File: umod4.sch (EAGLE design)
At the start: 73 parts, among them IC3 27C256-FEED-THRU, J1 DMSAT-SF-PEJ, J2 10118194-0001LF, J4 CORTEX_DEBUG-PTH, J5 C160394/JST BM08B-SRSS, J6 CORTEX_DEBUG-PTH, M1 RPi Pico W, M2 Generic single-sided NEO-8, Q1 C10487/SI2301CDS, Q2 C2150/SS8050, U1 C113281/74LVC541, U2 C6091/74LVC4245, U3 C113281/74LVC541, U4 C2040/RP2040, U5 C97521/W25Q128JVSIQ, U6 C10428/74LVC2G04, U7 C10428/74LVC2G04, Y1 C9002/12MHz

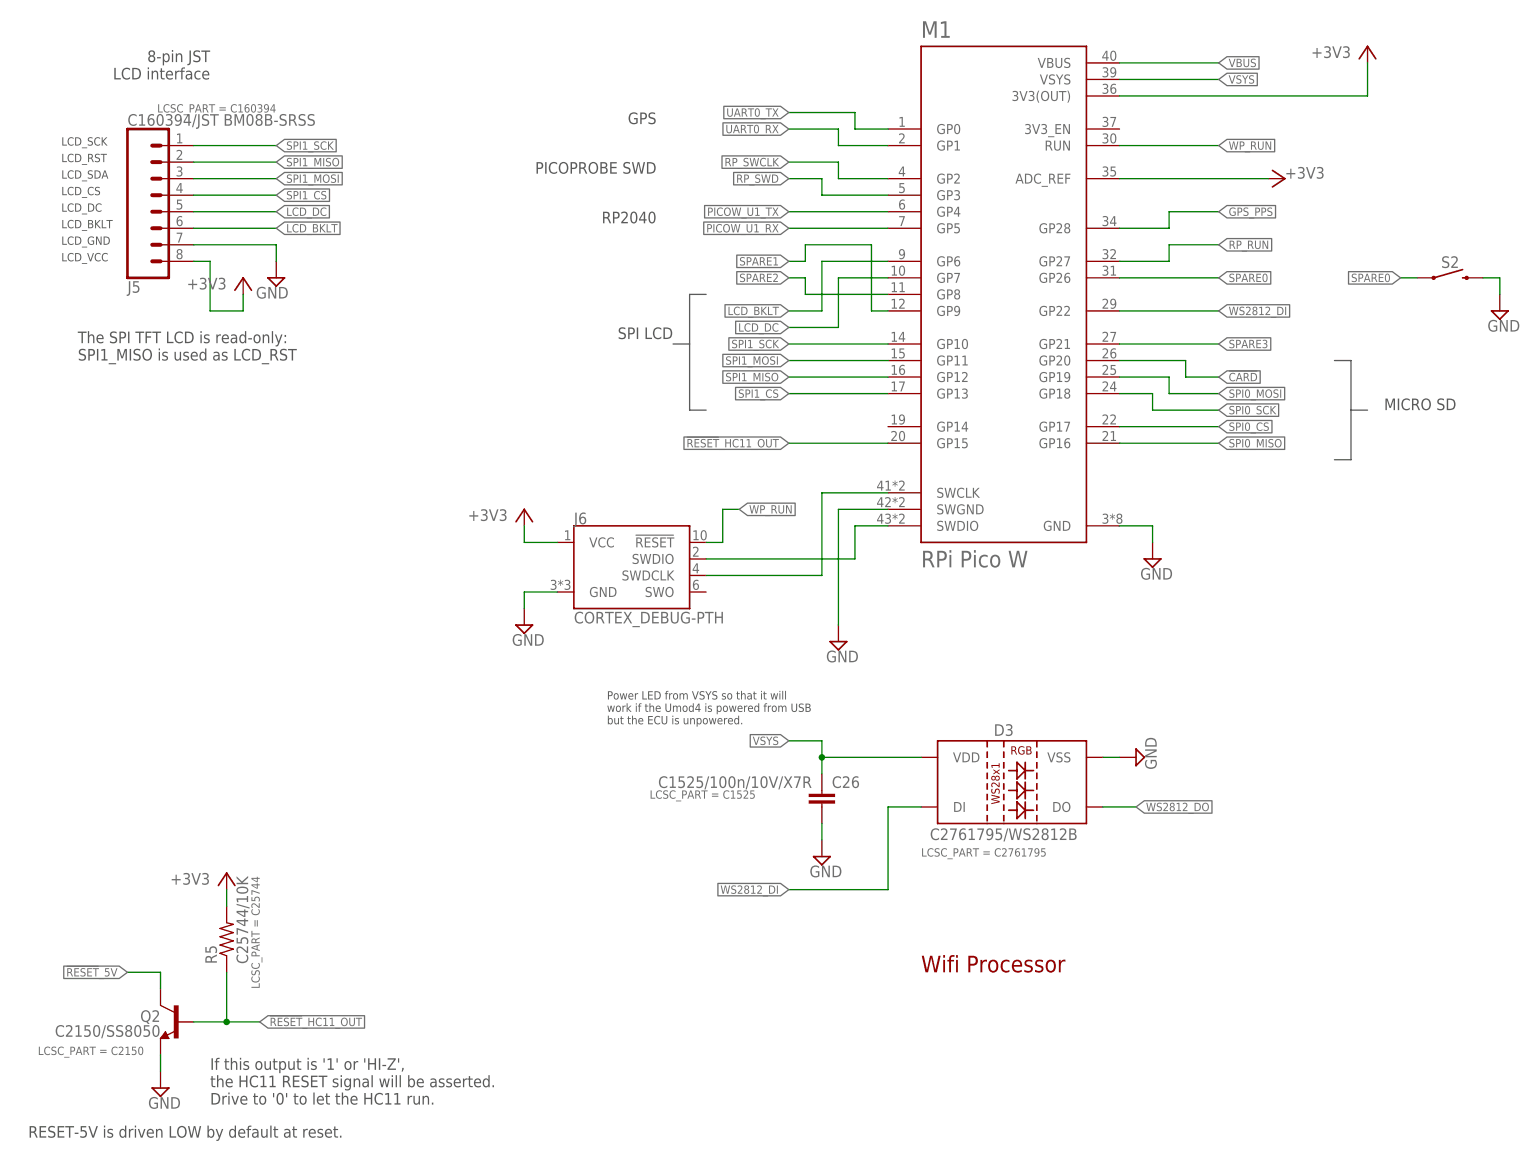
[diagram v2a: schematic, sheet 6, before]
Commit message: Added WP squid pins
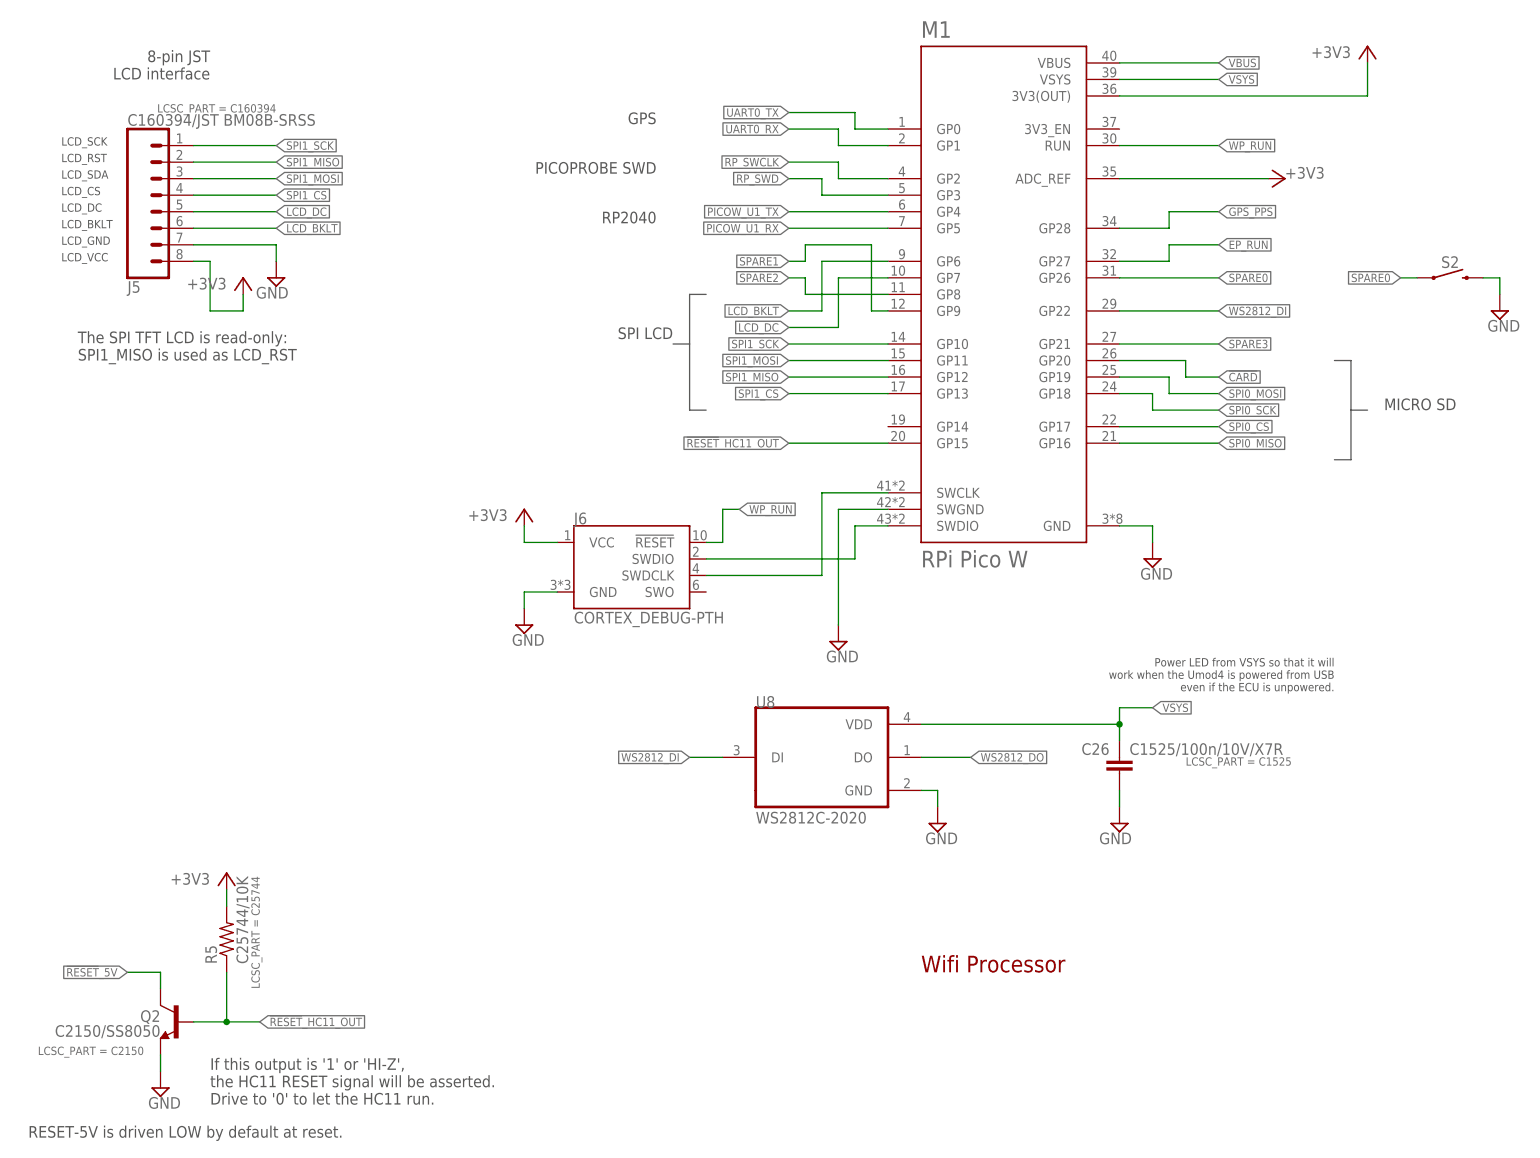
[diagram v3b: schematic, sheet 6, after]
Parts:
- removed D3: C2761795/WS2812B, SparkFun-LED:WS2812B
- added U8: WS2812C-2020, robins-v7:WS2812-2020
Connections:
- net RP_RUN renamed EP_RUN
- net GND: now also U8.GND; no longer D3.VSS
- net VSYS: now also U8.VDD; no longer D3.VDD
- net WS2812_DI: now also U8.DI; no longer D3.DI
- net WS2812_DO: now also U8.DO; no longer D3.DO
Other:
- note added: "Power LED from VSYS so that it will work when the Umod4 is powered from USB even if the ECU is unpowered."
- note removed: "Power LED from VSYS so that it will work if the Umod4 is powered from USB but the ECU is unpowered."
- moved on the sheet: C26
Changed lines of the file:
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@@
 <part name="SUPPLY21" library="supply2" deviceset="GND" device=""/>
 <part name="+3V19" library="supply1" deviceset="+3V3" device=""/>
-<part name="V13" library="supply2" deviceset="GND" device=""/>
-<part name="D3" library="SparkFun-LED" deviceset="WS2812B" device="" value="C2761795/WS2812B">
-<attribute name="LCSC_PART" value="C2761795"/>
-</part>
 <part name="C26" library="SparkFun-03-01-2010" deviceset="CAP" device="0402-CAP" value="C1525/100n/10V/X7R">
 <attribute name="LCSC_PART" value="C1525"/>
@@
 <part name="V30" library="supply2" deviceset="GND" device=""/>
 <part name="+3V24" library="supply1" deviceset="+3V3" device=""/>
+<part name="U8" library="robins-v7" deviceset="WS2812" device="-2020" value="WS2812C-2020"/>
+<part name="V41" library="supply2" deviceset="GND" device=""/>
 </parts>
 <sheets>
@@
 </segment>
 </net>
-<net name="RP_RUN" class="0">
+<net name="EP_RUN" class="0">
 <segment>
 <wire x1="119.38" y1="73.66" x2="104.14" y2="73.66" width="0.1524" layer="91"/>
@@
 the HC11 RESET signal will be asserted.
 Drive to '0' to let the HC11 run.</text>
-<text x="101.6" y="66.04" size="1.27" layer="97">Power LED from VSYS so that it will
-work if the Umod4 is powered from USB
-but the ECU is unpowered.</text>
+<text x="213.36" y="71.12" size="1.27" layer="97" rot="MR0">Power LED from VSYS so that it will
+work when the Umod4 is powered from USB
+even if the ECU is unpowered.</text>
 <text x="20.32" y="121.92" size="1.778" layer="97">The SPI TFT LCD is read-only:
 SPI1_MISO is used as LCD_RST</text>
@@
 <attribute name="VALUE" x="43.18" y="134.62" size="1.778" layer="96" rot="R180"/>
 </instance>
-<instance part="V13" gate="GND" x="182.88" y="60.96" rot="R90"/>
-<instance part="D3" gate="G$1" x="165.1" y="55.88">
-<attribute name="LCSC_PART" x="149.86" y="45.72" size="1.27" layer="96" display="both"/>
-</instance>
-<instance part="C26" gate="G$1" x="134.62" y="53.34" smashed="yes">
-<attribute name="NAME" x="136.144" y="56.261" size="1.778" layer="95"/>
-<attribute name="VALUE" x="133.096" y="58.039" size="1.778" layer="96" rot="R180"/>
-<attribute name="LCSC_PART" x="124.46" y="55.88" size="1.27" layer="96" rot="R180" display="both"/>
-</instance>
-<instance part="V34" gate="GND" x="134.62" y="45.72"/>
+<instance part="C26" gate="G$1" x="180.34" y="58.42" smashed="yes" rot="MR0">
+<attribute name="NAME" x="178.816" y="61.341" size="1.778" layer="95" rot="MR0"/>
+<attribute name="VALUE" x="181.864" y="63.119" size="1.778" layer="96" rot="MR180"/>
+<attribute name="LCSC_PART" x="190.5" y="60.96" size="1.27" layer="96" rot="MR180" display="both"/>
+</instance>
+<instance part="V34" gate="GND" x="180.34" y="50.8" rot="MR0"/>
 <instance part="Q2" gate="G$1" x="35.56" y="20.32" rot="MR0">
 <attribute name="LCSC_PART" x="30.48" y="15.24" size="1.27" layer="96" rot="MR0" display="both"/>
@@
 <attribute name="VALUE" x="205.74" y="149.86" size="1.778" layer="96"/>
 </instance>
+<instance part="U8" gate="G$1" x="134.62" y="60.96"/>
+<instance part="V41" gate="GND" x="152.4" y="50.8"/>
 </instances>
 <busses>
@@
 </segment>
 <segment>
-<wire x1="177.8" y1="60.96" x2="180.34" y2="60.96" width="0.1524" layer="91"/>
-<pinref part="V13" gate="GND" pin="GND"/>
-<pinref part="D3" gate="G$1" pin="VSS"/>
-</segment>
-<segment>
 <pinref part="C26" gate="G$1" pin="2"/>
-<wire x1="134.62" y1="50.8" x2="134.62" y2="48.26" width="0.1524" layer="91"/>
+<wire x1="180.34" y1="55.88" x2="180.34" y2="53.34" width="0.1524" layer="91"/>
 <pinref part="V34" gate="GND" pin="GND"/>
 </segment>
@@
 <wire x1="88.9" y1="86.36" x2="88.9" y2="83.82" width="0.1524" layer="91"/>
 <pinref part="V30" gate="GND" pin="GND"/>
+</segment>
+<segment>
+<pinref part="U8" gate="G$1" pin="GND"/>
+<wire x1="149.86" y1="55.88" x2="152.4" y2="55.88" width="0.1524" layer="91"/>
+<wire x1="152.4" y1="55.88" x2="152.4" y2="53.34" width="0.1524" layer="91"/>
+<pinref part="V41" gate="GND" pin="GND"/>
 </segment>
 </net>
@@
 </segment>
 </net>
-<net name="RP_RUN" class="0">
+<net name="EP_RUN" class="0">
 <segment>
 <label x="195.58" y="139.7" size="1.27" layer="95" xref="yes"/>
@@
 <segment>
 <pinref part="C26" gate="G$1" pin="1"/>
-<wire x1="134.62" y1="58.42" x2="134.62" y2="60.96" width="0.1524" layer="91"/>
-<pinref part="D3" gate="G$1" pin="VDD"/>
-<wire x1="134.62" y1="60.96" x2="149.86" y2="60.96" width="0.1524" layer="91"/>
-<wire x1="134.62" y1="60.96" x2="134.62" y2="63.5" width="0.1524" layer="91"/>
-<junction x="134.62" y="60.96"/>
-<wire x1="134.62" y1="63.5" x2="129.54" y2="63.5" width="0.1524" layer="91"/>
-<label x="129.54" y="63.5" size="1.27" layer="95" rot="R180" xref="yes"/>
+<wire x1="180.34" y1="63.5" x2="180.34" y2="66.04" width="0.1524" layer="91"/>
+<wire x1="180.34" y1="66.04" x2="180.34" y2="68.58" width="0.1524" layer="91"/>
+<junction x="180.34" y="66.04"/>
+<wire x1="180.34" y1="68.58" x2="185.42" y2="68.58" width="0.1524" layer="91"/>
+<label x="185.42" y="68.58" size="1.27" layer="95" rot="MR180" xref="yes"/>
+<pinref part="U8" gate="G$1" pin="VDD"/>
+<wire x1="180.34" y1="66.04" x2="149.86" y2="66.04" width="0.1524" layer="91"/>
 </segment>
 </net>
@@
 <net name="WS2812_DI" class="0">
 <segment>
-<wire x1="149.86" y1="53.34" x2="144.78" y2="53.34" width="0.1524" layer="91"/>
-<wire x1="144.78" y1="53.34" x2="144.78" y2="40.64" width="0.1524" layer="91"/>
-<wire x1="144.78" y1="40.64" x2="129.54" y2="40.64" width="0.1524" layer="91"/>
-<label x="129.54" y="40.64" size="1.27" layer="95" rot="R180" xref="yes"/>
-<pinref part="D3" gate="G$1" pin="DI"/>
+<wire x1="119.38" y1="60.96" x2="114.3" y2="60.96" width="0.1524" layer="91"/>
+<label x="114.3" y="60.96" size="1.27" layer="95" rot="R180" xref="yes"/>
+<pinref part="U8" gate="G$1" pin="DI"/>
 </segment>
 <segment>
@@
 <net name="WS2812_DO" class="0">
 <segment>
-<pinref part="D3" gate="G$1" pin="DO"/>
-<wire x1="177.8" y1="53.34" x2="182.88" y2="53.34" width="0.1524" layer="91"/>
-<label x="182.88" y="53.34" size="1.27" layer="95" xref="yes"/>
-</segment>
-</net>
+<label x="157.48" y="60.96" size="1.27" layer="95" xref="yes"/>
+<pinref part="U8" gate="G$1" pin="DO"/>
+<wire x1="149.86" y1="60.96" x2="157.48" y2="60.96" width="0.1524" layer="91"/>
+</segment>
+</net>

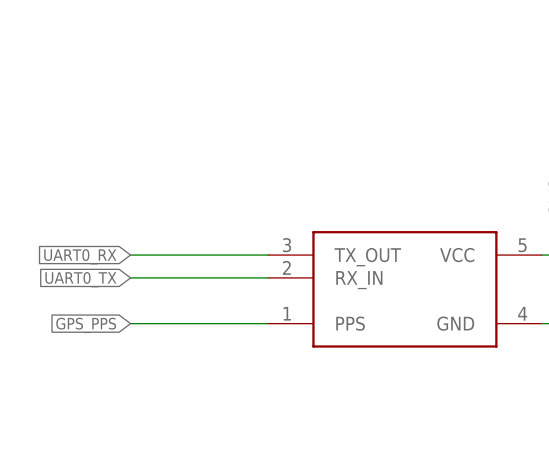
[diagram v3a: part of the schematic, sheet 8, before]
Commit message: Pullup Stops GPS From Disabling Its UART
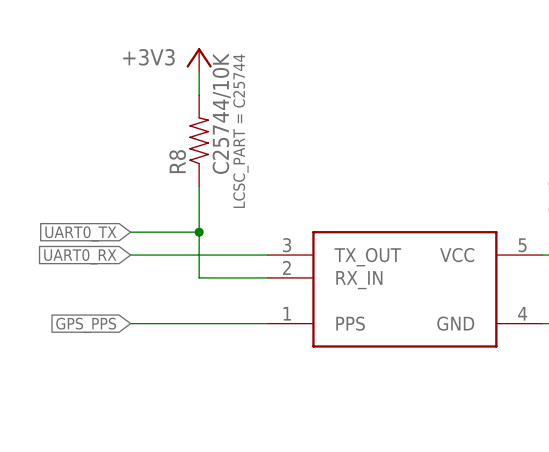
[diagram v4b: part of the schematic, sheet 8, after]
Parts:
- added R8: C25744/10K, SparkFun-03-01-2010:RESISTOR0402-RES
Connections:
- net +3V3: now also R8.2
- net UART0_TX: now also R8.1
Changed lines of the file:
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@@
 <setting verticaltext="up"/>
 </settings>
-<grid distance="0.1" unitdist="inch" unit="inch" style="lines" multiple="1" display="no" altdistance="0.01" altunitdist="inch" altunit="inch"/>
+<grid distance="0.1" unitdist="inch" unit="inch" style="lines" multiple="1" display="yes" altdistance="0.01" altunitdist="inch" altunit="inch"/>
 <layers>
 <layer number="1" name="Top" color="4" fill="1" visible="no" active="no"/>
@@
 <part name="U8" library="robins-v7" deviceset="WS2812" device="-2020" value="WS2812C-2020"/>
 <part name="V41" library="supply2" deviceset="GND" device=""/>
+<part name="+3V20" library="supply1" deviceset="+3V3" device=""/>
+<part name="R8" library="SparkFun-03-01-2010" deviceset="RESISTOR" device="0402-RES" value="C25744/10K">
+<attribute name="LCSC_PART" value="C25744"/>
+</part>
 </parts>
 <sheets>
@@
 <text x="17.78" y="139.7" size="1.27" layer="97">LCD_GND</text>
 <text x="17.78" y="137.16" size="1.27" layer="97">LCD_VCC</text>
+<wire x1="139.7" y1="157.48" x2="140.97" y2="158.75" width="0.1524" layer="97"/>
+<wire x1="139.7" y1="157.48" x2="140.97" y2="156.21" width="0.1524" layer="97"/>
+<wire x1="139.7" y1="156.21" x2="140.97" y2="154.94" width="0.1524" layer="97"/>
+<wire x1="140.97" y1="154.94" x2="139.7" y2="153.67" width="0.1524" layer="97"/>
 </plain>
 <instances>
@@
 <segment>
 <label x="129.54" y="160.02" size="1.27" layer="95" rot="R180" xref="yes"/>
-<wire x1="139.7" y1="160.02" x2="129.54" y2="160.02" width="0.1524" layer="91"/>
-<wire x1="139.7" y1="160.02" x2="139.7" y2="157.48" width="0.1524" layer="91"/>
+<wire x1="137.16" y1="160.02" x2="129.54" y2="160.02" width="0.1524" layer="91"/>
+<wire x1="137.16" y1="160.02" x2="137.16" y2="157.48" width="0.1524" layer="91"/>
 <pinref part="M1" gate="G$1" pin="GP0"/>
-<wire x1="139.7" y1="157.48" x2="144.78" y2="157.48" width="0.1524" layer="91"/>
+<wire x1="137.16" y1="157.48" x2="144.78" y2="157.48" width="0.1524" layer="91"/>
 </segment>
 </net>
@@
 <segment>
 <label x="129.54" y="157.48" size="1.27" layer="95" rot="R180" xref="yes"/>
-<wire x1="137.16" y1="157.48" x2="129.54" y2="157.48" width="0.1524" layer="91"/>
-<wire x1="137.16" y1="157.48" x2="137.16" y2="154.94" width="0.1524" layer="91"/>
+<wire x1="134.62" y1="157.48" x2="129.54" y2="157.48" width="0.1524" layer="91"/>
+<wire x1="134.62" y1="157.48" x2="134.62" y2="154.94" width="0.1524" layer="91"/>
 <pinref part="M1" gate="G$1" pin="GP1"/>
-<wire x1="137.16" y1="154.94" x2="144.78" y2="154.94" width="0.1524" layer="91"/>
+<wire x1="134.62" y1="154.94" x2="144.78" y2="154.94" width="0.1524" layer="91"/>
 </segment>
 </net>
@@
 <instance part="V33" gate="GND" x="137.16" y="101.6"/>
 <instance part="+3V18" gate="G$1" x="137.16" y="121.92"/>
+<instance part="+3V20" gate="G$1" x="93.98" y="137.16" smashed="yes">
+<attribute name="VALUE" x="91.44" y="137.16" size="1.778" layer="96" rot="R180"/>
+</instance>
+<instance part="R8" gate="G$1" x="93.98" y="127" rot="R90">
+<attribute name="LCSC_PART" x="99.06" y="119.38" size="1.27" layer="96" rot="R90" display="both"/>
+</instance>
 </instances>
 <busses>
@@
 <wire x1="137.16" y1="114.3" x2="132.08" y2="114.3" width="0.1524" layer="91"/>
 </segment>
+<segment>
+<wire x1="93.98" y1="132.08" x2="93.98" y2="134.62" width="0.1524" layer="91"/>
+<pinref part="+3V20" gate="G$1" pin="+3V3"/>
+<pinref part="R8" gate="G$1" pin="2"/>
+</segment>
 </net>
 <net name="GND" class="0">
@@
 <segment>
 <pinref part="M2" gate="G$1" pin="RX_IN"/>
-<wire x1="101.6" y1="111.76" x2="86.36" y2="111.76" width="0.1524" layer="91"/>
-<label x="86.36" y="111.76" size="1.27" layer="95" rot="R180" xref="yes"/>
+<wire x1="101.6" y1="111.76" x2="93.98" y2="111.76" width="0.1524" layer="91"/>
+<wire x1="93.98" y1="111.76" x2="93.98" y2="116.84" width="0.1524" layer="91"/>
+<wire x1="93.98" y1="116.84" x2="86.36" y2="116.84" width="0.1524" layer="91"/>
+<label x="86.36" y="116.84" size="1.27" layer="95" rot="R180" xref="yes"/>
+<pinref part="R8" gate="G$1" pin="1"/>
+<wire x1="93.98" y1="116.84" x2="93.98" y2="121.92" width="0.1524" layer="91"/>
+<junction x="93.98" y="116.84"/>
 </segment>
 </net>

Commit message: Latest updates. See ChangeList.md.
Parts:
- added C13: 4.7uF/25V, robins-v7:CAP-0603
- added C28, C29: 0.1uF/25V, robins-v7:CAP-0603
- added C30, C31: 10uF/10V, robins-v7:CAP-0805
- added D3, D4: 1A/23V/620mV, SparkFun-DiscreteSemi:DIODE-SCHOTTKY-BAT20J
- added L1: 22uH, robins-v7:INDUCTOR-PWRCJAING-FHD4020
- added R17: 22K, robins-v7:RESISTOR-0603
- added R19: 10K, robins-v7:RESISTOR-0603
- added R9: 51K, robins-v7:RESISTOR-0603
- added U9: TPS560430X, robins-v7:TPS560430-SOT23-6
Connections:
- new net +12_US: C13.1, C28.1, U9.VIN
- new net +5_SW: C30.1, C31.1, D1.A, L1.2, Q1.D, R9.2
- new net KEEP_ALIVE: D4.A
- new net N$16: R17.2, R9.1, U9.FB
- new net N$23: D3.C, D4.C, R19.2, U9.EN
- new net N$3: C29.1, U9.CB
- new net SW: C29.2, L1.1, U9.SW
- net +5V: now also D3.A; no longer D1.A, Q1.D
- net GND: now also C13.2, C28.2, C30.2, C31.2, R17.1, R19.1, U9.GND
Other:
- note added: "'1' or 'HI-Z' asserts HC11 !RESET!. '0' lets the HC11 run."
- note added: "Umod4 Power Supply Operation 1. Umod4 uses the PicoW as a power supply a. Umod4 supplies 5V to PicoW as VSYS b. PicoW converts the VSYS to +3V3, used to power the Umod4 b. If PicoW is not present +3V3, can be injected via JP2 to power EP 2. VSYS is supplied to PicoW by: a. Plugging USB power into the PicoW (even with ignition OFF) b. Turning ignition key is ON i. Presence of ECU +5V supply enable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"
- note added: "VBUS comes from PicoW USB connector"
- note added: "VSYS feeds the PicoW DC-DC converter that generates +3V3 to the entire umod4 board"
- note removed: "+5V from the ECU"
- note removed: "If this output is '1' or 'HI-Z', the HC11 RESET signal will be asserted. Drive to '0' to let the HC11 run."
- note removed: "RESET-5V is driven LOW by default at reset."
- note removed: "The Ultramod4 is powered from the ECU +5V supply by default. If USB power is applied to the Pico, the Ultramod board will be powered even if the ECU is OFF."
- note removed: "VBUS comes from PicoW USB"
- note removed: "VSYS feeds the PicoW DC-DC converter"
- moved on the sheet: C15, C17, C18, C19, C20, C21, C8, D1, D2, J2, J4, JP2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
